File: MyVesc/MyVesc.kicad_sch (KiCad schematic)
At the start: 20 parts, among them J1 CAN, J14 Pull_up, J2 Conn_01x08, J4 Conn_01x03, P4 HALL/Encoder

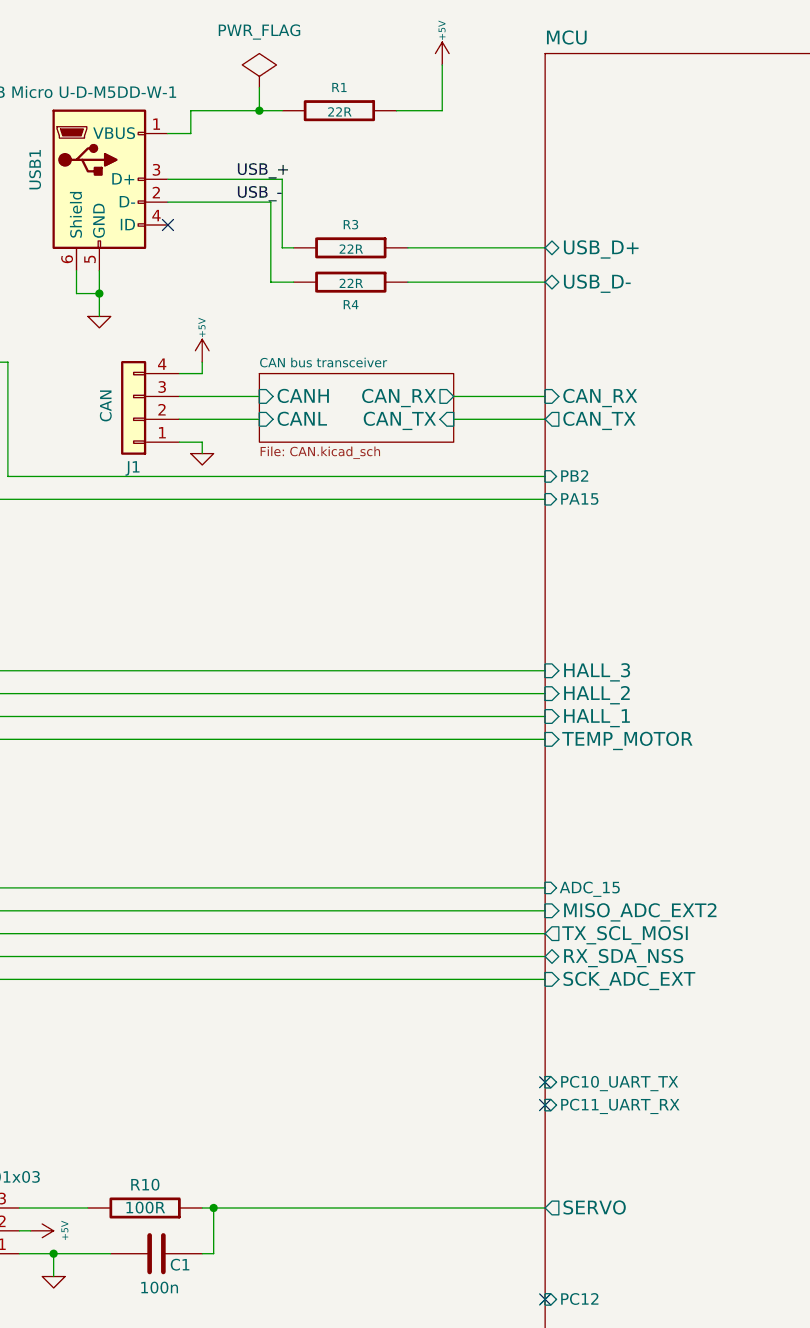
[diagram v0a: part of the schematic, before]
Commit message: routerd logic board
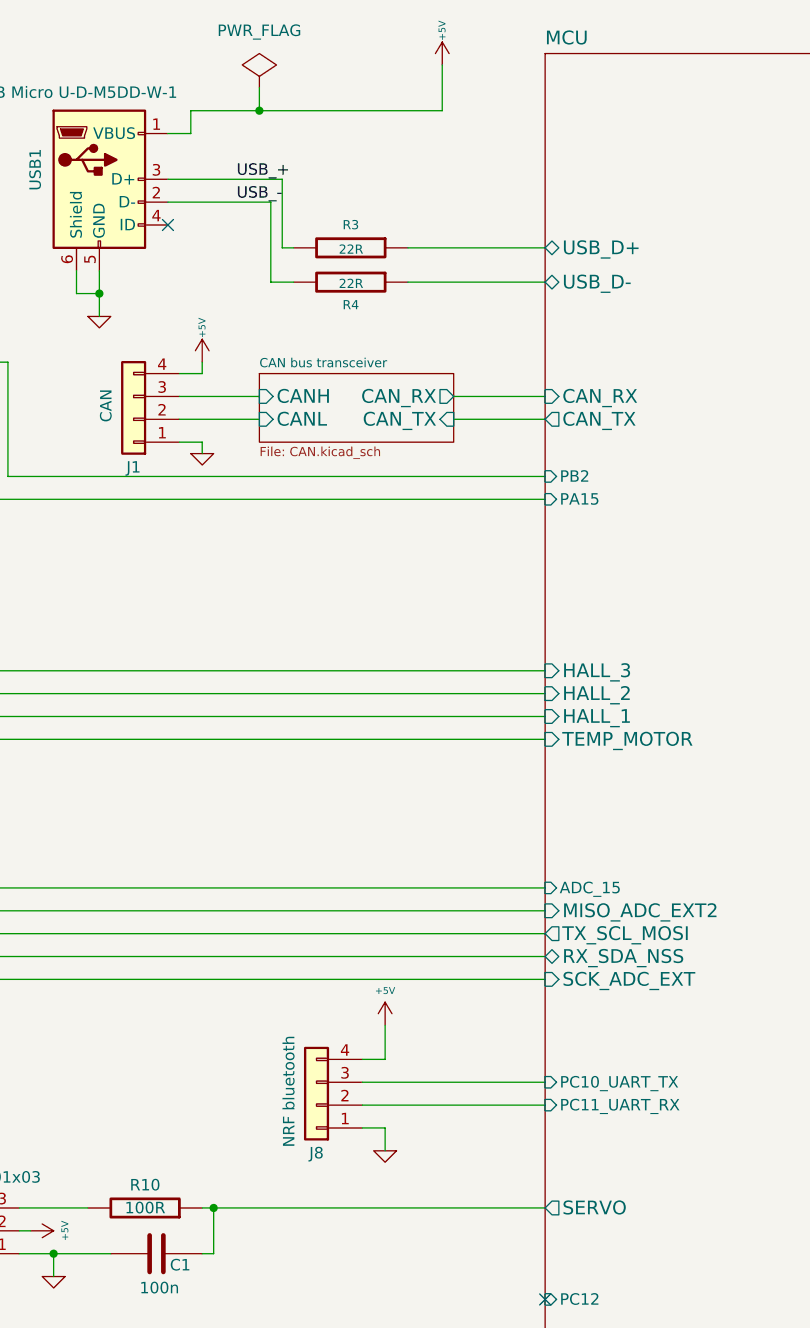
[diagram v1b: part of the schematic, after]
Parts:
- removed R1: 22R, Resistor_SMD:R_0603_1608Metric, symbol BLDC_4-rescue:R-RESCUE-BLDC_4
- added J8: NRF bluetooth, Connector_JST:JST_PH_B4B-PH-K_1x04_P2.00mm_Vertical, symbol Connector_Generic:Conn_01x04
- USB1: footprint Connector_USB:USB_Micro-B_Wuerth_614105150721_Vertical -> Connector_USB:USB_Mini-B_Lumberg_2486_01_Horizontal
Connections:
- net +5V: now also USB1.1 (VBUS), J8.4 (Pin_4)
- net GND: now also J8.1 (Pin_1)
- net MCU/PC10_UART_TX: now also J8.3 (Pin_3)
- net MCU/PC11_UART_RX: now also J8.2 (Pin_2)
- no-connect marks 4 -> 2
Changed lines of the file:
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@@
 	)
 	(no_connect
-		(at 127 133.35)
-	)
-	(no_connect
-		(at 127 135.89)
-	)
-	(no_connect
 		(at 127 157.48)
 	)
@@
 	(wire
 		(pts
+			(xy 106.68 135.89) (xy 127 135.89)
+		)
+		(stroke
+			(width 0)
+			(type default)
+		)
+	)
+	(wire
+		(pts
 			(xy 46.99 87.63) (xy 50.8 87.63)
 		)
@@
 	(wire
 		(pts
-			(xy 110.49 25.4) (xy 115.57 25.4)
+			(xy 191.77 43.18) (xy 198.12 43.18)
 		)
 		(stroke
@@
 	(wire
 		(pts
-			(xy 191.77 43.18) (xy 198.12 43.18)
+			(xy 109.22 138.43) (xy 109.22 140.97)
 		)
 		(stroke
@@
 	(wire
 		(pts
+			(xy 109.22 130.81) (xy 109.22 127)
+		)
+		(stroke
+			(width 0)
+			(type default)
+		)
+	)
+	(wire
+		(pts
 			(xy 88.9 54.61) (xy 88.9 53.34)
 		)
@@
 	(wire
 		(pts
-			(xy 97.79 25.4) (xy 95.25 25.4)
+			(xy 95.25 25.4) (xy 115.57 25.4)
 		)
 		(stroke
@@
 	(wire
 		(pts
+			(xy 106.68 130.81) (xy 109.22 130.81)
+		)
+		(stroke
+			(width 0)
+			(type default)
+		)
+	)
+	(wire
+		(pts
+			(xy 106.68 133.35) (xy 127 133.35)
+		)
+		(stroke
+			(width 0)
+			(type default)
+		)
+	)
+	(wire
+		(pts
 			(xy 250.19 134.62) (xy 257.81 134.62)
 		)
@@
 	(wire
 		(pts
+			(xy 106.68 138.43) (xy 109.22 138.43)
+		)
+		(stroke
+			(width 0)
+			(type default)
+		)
+	)
+	(wire
+		(pts
 			(xy 191.77 45.72) (xy 198.12 45.72)
 		)
@@
 			)
 		)
-		(property "Footprint" "Connector_USB:USB_Micro-B_Wuerth_614105150721_Vertical"
+		(property "Footprint" "Connector_USB:USB_Mini-B_Lumberg_2486_01_Horizontal"
 			(at 77.978 54.864 0)
 			(effects
@@
 	)
 	(symbol
+		(lib_id "BLDC_4-rescue:+5V")
+		(at 109.22 127 0)
+		(unit 1)
+		(exclude_from_sim no)
+		(in_bom yes)
+		(on_board yes)
+		(dnp no)
+		(property "Reference" "#PWR076"
+			(at 109.22 124.714 0)
+			(effects
+				(font
+					(size 0.508 0.508)
+				)
+				(hide yes)
+			)
+		)
+		(property "Value" "+5V"
+			(at 109.22 123.19 0)
+			(effects
+				(font
+					(size 0.762 0.762)
+				)
+			)
+		)
+		(property "Footprint" ""
+			(at 109.22 127 0)
+			(effects
+				(font
+					(size 1.524 1.524)
+				)
+				(hide yes)
+			)
+		)
+		(property "Datasheet" ""
+			(at 109.22 127 0)
+			(effects
+				(font
+					(size 1.524 1.524)
+				)
+				(hide yes)
+			)
+		)
+		(property "Description" ""
+			(at 109.22 127 0)
+			(effects
+				(font
+					(size 1.27 1.27)
+				)
+				(hide yes)
+			)
+		)
+		(pin "1"
+		)
+		(instances
+			(project "MyVesc"
+				(path "/b7d1d049-1490-46e4-83b7-ec5dff08d2d8"
+					(reference "#PWR076")
+					(unit 1)
+				)
+			)
+		)
+	)
+	(symbol
 		(lib_id "BLDC_4-rescue:C-RESCUE-BLDC_4")
 		(at 83.82 152.4 90)
@@
 	)
 	(symbol
+		(lib_id "Connector_Generic:Conn_01x04")
+		(at 101.6 135.89 180)
+		(unit 1)
+		(exclude_from_sim no)
+		(in_bom yes)
+		(on_board yes)
+		(dnp no)
+		(property "Reference" "J8"
+			(at 101.6 141.224 0)
+			(effects
+				(font
+					(size 1.27 1.27)
+				)
+			)
+		)
+		(property "Value" "NRF bluetooth"
+			(at 98.552 134.366 90)
+			(effects
+				(font
+					(size 1.27 1.27)
+				)
+			)
+		)
+		(property "Footprint" "Connector_JST:JST_PH_B4B-PH-K_1x04_P2.00mm_Vertical"
+			(at 101.6 135.89 0)
+			(effects
+				(font
+					(size 1.27 1.27)
+				)
+				(hide yes)
+			)
+		)
+		(property "Datasheet" "~"
+			(at 101.6 135.89 0)
+			(effects
+				(font
+					(size 1.27 1.27)
+				)
+				(hide yes)
+			)
+		)
+		(property "Description" "Generic connector, single row, 01x04, script generated (kicad-library-utils/schlib/autogen/connector/)"
+			(at 101.6 135.89 0)
+			(effects
+				(font
+					(size 1.27 1.27)
+				)
+				(hide yes)
+			)
+		)
+		(pin "1"
+		)
+		(pin "4"
+		)
+		(pin "2"
+		)
+		(pin "3"
+		)
+		(instances
+			(project "MyVesc"
+				(path "/b7d1d049-1490-46e4-83b7-ec5dff08d2d8"
+					(reference "J8")
+					(unit 1)
+				)
+			)
+		)
+	)
+	(symbol
 		(lib_id "BLDC_4-rescue:PWR_FLAG")
 		(at 21.59 165.1 180)
@@
 	)
 	(symbol
+		(lib_id "BLDC_4-rescue:GND-RESCUE-BLDC_4")
+		(at 109.22 140.97 0)
+		(mirror y)
+		(unit 1)
+		(exclude_from_sim no)
+		(in_bom yes)
+		(on_board yes)
+		(dnp no)
+		(property "Reference" "#PWR077"
+			(at 109.22 140.97 0)
+			(effects
+				(font
+					(size 0.762 0.762)
+				)
+				(hide yes)
+			)
+		)
+		(property "Value" "GND"
+			(at 109.22 142.748 0)
+			(effects
+				(font
+					(size 0.762 0.762)
+				)
+				(hide yes)
+			)
+		)
+		(property "Footprint" ""
+			(at 109.22 140.97 0)
+			(effects
+				(font
+					(size 1.524 1.524)
+				)
+				(hide yes)
+			)
+		)
+		(property "Datasheet" ""
+			(at 109.22 140.97 0)
+			(effects
+				(font
+					(size 1.524 1.524)
+				)
+				(hide yes)
+			)
+		)
+		(property "Description" ""
+			(at 109.22 140.97 0)
+			(effects
+				(font
+					(size 1.27 1.27)
+				)
+				(hide yes)
+			)
+		)
+		(pin "1"
+		)
+		(instances
+			(project "MyVesc"
+				(path "/b7d1d049-1490-46e4-83b7-ec5dff08d2d8"
+					(reference "#PWR077")
+					(unit 1)
+				)
+			)
+		)
+	)
+	(symbol
 		(lib_id "BLDC_4-rescue:+5V")
 		(at 20.32 53.34 0)
@@
 					(unit 1)
 				)
-			)
-		)
-	)
-	(symbol
-		(lib_id "BLDC_4-rescue:R-RESCUE-BLDC_4")
-		(at 104.14 25.4 270)
-		(unit 1)
-		(exclude_from_sim no)
-		(in_bom yes)
-		(on_board yes)
-		(dnp no)
-		(property "Reference" "R1"
-			(at 104.14 22.86 90)
-			(effects
-				(font
-					(size 1.016 1.016)
-				)
-			)
-		)
-		(property "Value" "22R"
-			(at 104.1654 25.5778 90)
-			(effects
-				(font
-					(size 1.016 1.016)
-				)
-			)
-		)
-		(property "Footprint" "Resistor_SMD:R_0603_1608Metric"
-			(at 104.14 23.622 90)
-			(effects
-				(font
-					(size 0.762 0.762)
-				)
-				(hide yes)
-			)
-		)
-		(property "Datasheet" ""
-			(at 104.14 25.4 0)
-			(effects
-				(font
-					(size 0.762 0.762)
-				)
-			)
-		)
-		(property "Description" ""
-			(at 104.14 25.4 0)
-			(effects
-				(font
-					(size 1.27 1.27)
-				)
-				(hide yes)
-			)
-		)
-		(pin "2"
-		)
-		(pin "1"
-		)
-		(instances
-			(project "MyVesc"
-				(path "/b7d1d049-1490-46e4-83b7-ec5dff08d2d8"
-					(reference "R1")
-					(unit 1)
-				)
